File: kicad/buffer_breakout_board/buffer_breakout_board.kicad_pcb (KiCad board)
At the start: 4 copper layers, 44.7 x 44.6 mm, 46 parts, among them J1 Power, J2 Vcca_select, J3 In_Hi, J4 In_Lo, J5 Out_Hi, J6 Out_Lo, J7 Vccb_select, J8 JST_SH_BM04B-SRSS-TB, J9 Signals, U1 MCP4725A2T-E/CH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

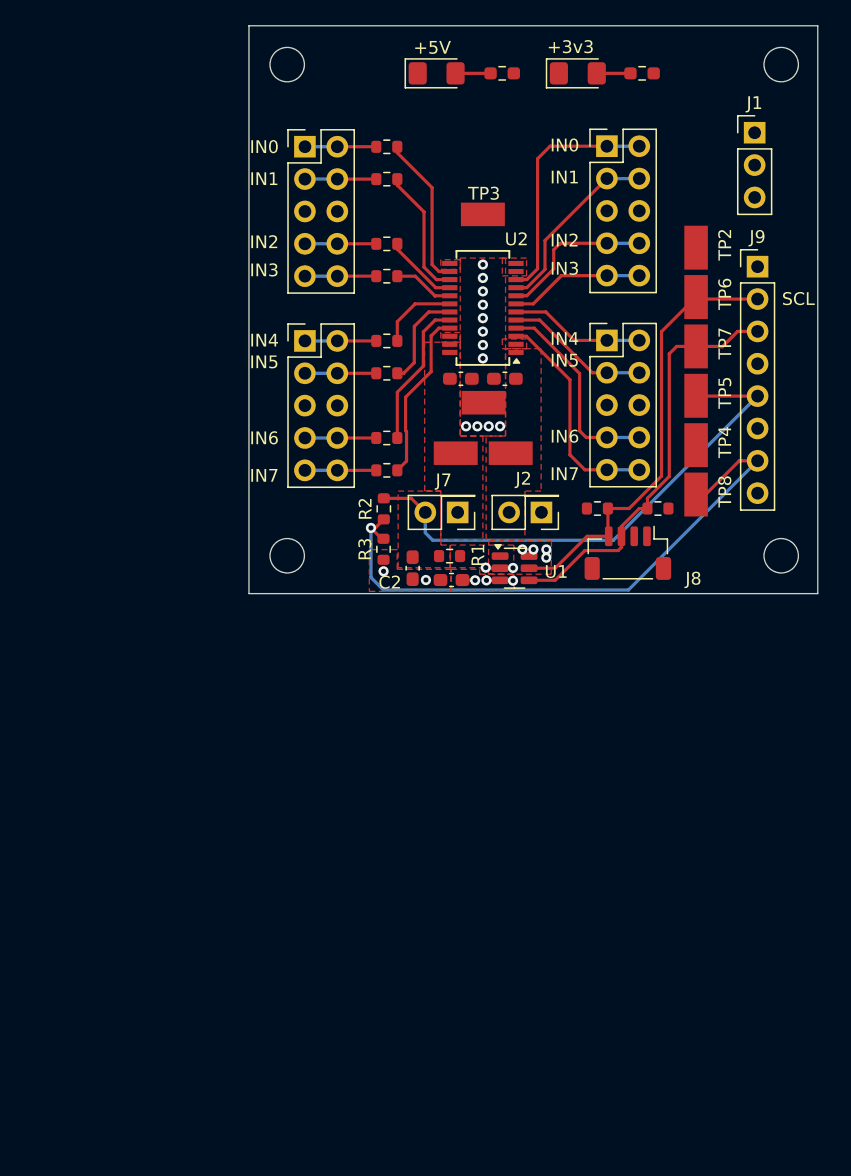
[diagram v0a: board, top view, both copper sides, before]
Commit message: renamed files, was working on wrong directory
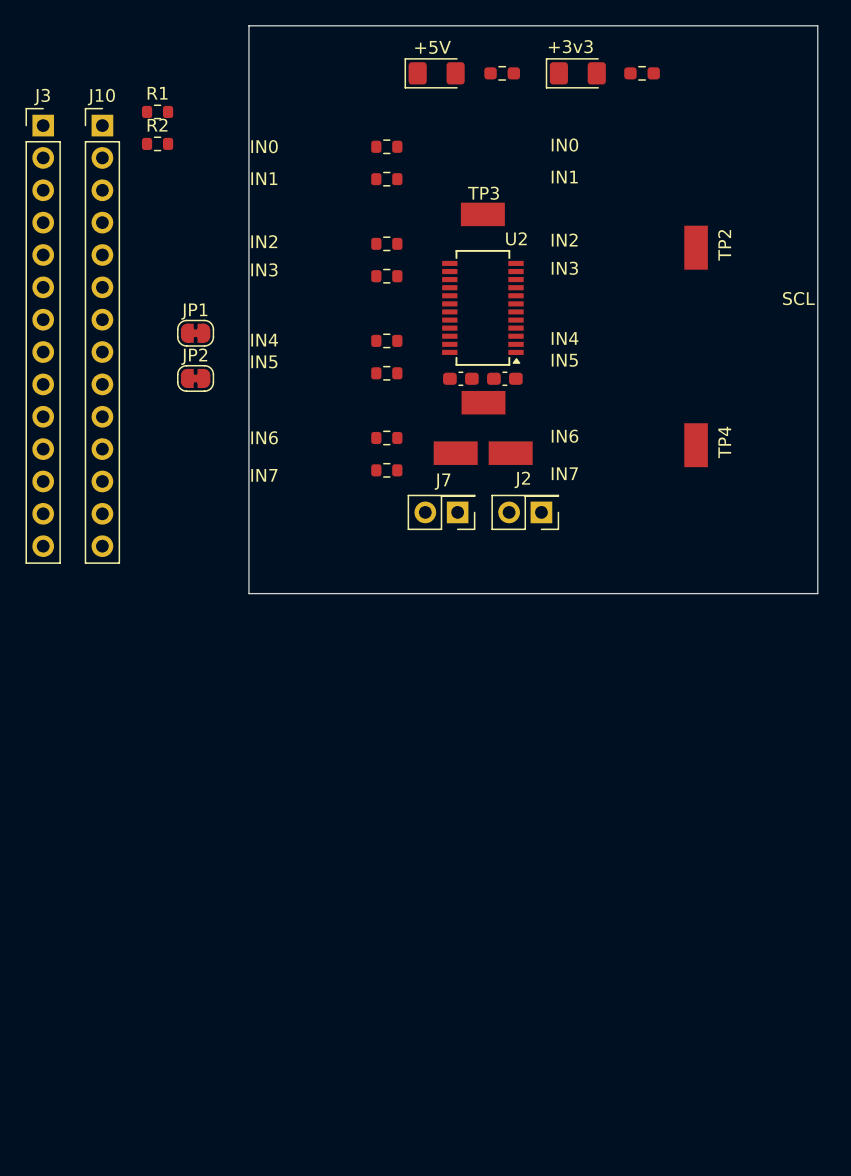
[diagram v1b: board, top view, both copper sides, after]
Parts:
- removed C1: 1u, Capacitor_SMD:C_0603_1608Metric_Pad1.08x0.95mm_HandSolder
- removed C2: 100n, Capacitor_SMD:C_0603_1608Metric_Pad1.08x0.95mm_HandSolder
- removed H1, H2, H3, H4: MountingHole, MountingHole:MountingHole_2.7mm
- removed J1: Power, Connector_PinHeader_2.54mm:PinHeader_1x03_P2.54mm_Vertical
- removed J4: In_Lo, Connector_PinHeader_2.54mm:PinHeader_2x05_P2.54mm_Vertical
- removed J5: Out_Hi, Connector_PinHeader_2.54mm:PinHeader_2x05_P2.54mm_Vertical
- removed J6: Out_Lo, Connector_PinHeader_2.54mm:PinHeader_2x05_P2.54mm_Vertical
- removed J8: JST_SH_BM04B-SRSS-TB, Connector_JST:JST_SH_BM04B-SRSS-TB_1x04-1MP_P1.00mm_Vertical
- removed J9: Signals, Connector_PinHeader_2.54mm:PinHeader_1x08_P2.54mm_Vertical
- removed R12, R13, R3: 10k, Resistor_SMD:R_0603_1608Metric
- removed TP5, TP6, TP7, TP8: TestPoint_Harwin, My Libraries:Harwin-S1751-46-Test-Point
- removed U1: MCP4725A2T-E/CH, Package_TO_SOT_SMD:SOT-23-6
- added J10: Data_In, Connector_PinHeader_2.54mm:PinHeader_1x14_P2.54mm_Vertical, F.Cu at (130.1, 83.3)
- added JP1: Jumper_2_Bridged, Jumper:SolderJumper-2_P1.3mm_Bridged_RoundedPad1.0x1.5mm, F.Cu at (137.5, 99.6)
- added JP2: Jumper_2_Bridged, Jumper:SolderJumper-2_P1.3mm_Bridged_RoundedPad1.0x1.5mm, F.Cu at (137.5, 103.2)
- D1: value 5V -> Vb
- D2: value 3v3 -> Va
- J3: value In_Hi -> Data_Out; footprint Connector_PinHeader_2.54mm:PinHeader_2x05_P2.54mm_Vertical -> Connector_PinHeader_2.54mm:PinHeader_1x14_P2.54mm_Vertical
- R1: value 0 -> 1k
- R2: value 10k -> 1k
- moved R1 41.7 mm to (134.5, 82.3), turned to 0 degrees
- moved R2 33.7 mm to (134.5, 84.8), turned to 0 degrees
- moved J3 26.6 mm to (125.5, 83.3)
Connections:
- J2 pad 1: +3V3 -> /Va_In
- J3 pad 1: /IN04 -> /Va_In
- J3 pad 10: /IN07 -> /BUF03
- J3 pad 2: /IN04 -> GND
- J3 pad 3: /IN05 -> /DIR
- J3 pad 4: /IN05 -> GND
- J3 pad 5: GND -> /BUF07
- J3 pad 6: GND -> /BUF06
- J3 pad 7: /IN06 -> /BUF05
- J3 pad 8: /IN06 -> /BUF04
- J3 pad 9: /IN07 -> GND
- J7 pad 2: /Vdac_out -> /Vb_In
- R1 pad 1: Net-(U1-VOUT) -> /DIR
- R1 pad 2: /Vdac_out -> GND
- R14 pad 1: +5V -> Net-(JP1-A)
- R15 pad 1: +3V3 -> Net-(JP2-A)
- R2 pad 1: /Vdac_half -> /OE
- R2 pad 2: /Vdac_out -> GND
- U2 pad 2: GND -> /DIR
- U2 pad 22: GND -> /OE
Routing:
- net /Vdac_half: track 47.4 -> 0.00 mm, vias 1 -> 0
- net /Vdac_out: track 41.2 -> 0.00 mm
- net /I2C1_SCL: track 34.8 -> 0.00 mm
- net /I2C1_SDA: track 33.1 -> 0.00 mm
- net /BUF00: track 19.1 -> 0.00 mm
- net /BUF07: track 17.5 -> 0.00 mm
- net /BUF06: track 15.9 -> 0.00 mm
- net /BUF01: track 14.6 -> 0.00 mm
- net /B7: track 13.4 -> 0.00 mm
- net /BUF02: track 12.3 -> 0.00 mm
- net /B0: track 12.0 -> 0.00 mm
- net /B6: track 11.6 -> 0.00 mm
- net /BUF05: track 11.4 -> 0.00 mm
- net /BUF04: track 10.6 -> 0.00 mm
- net /BUF03: track 10.6 -> 0.00 mm
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- removed copper zone on F.Cu, net +5V
- removed copper zone on F.Cu, net /Vdac_out
- removed copper zone on F.Cu, net GND
- removed copper zone on In1.Cu, net GND
- removed copper zone on F.Cu, net Net-(U1-VOUT)
- removed copper zone on F.Cu, net Vcca
- removed copper zone on F.Cu, net Vccb
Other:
- copper layers 4 -> 2

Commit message: floor planning attempt 1
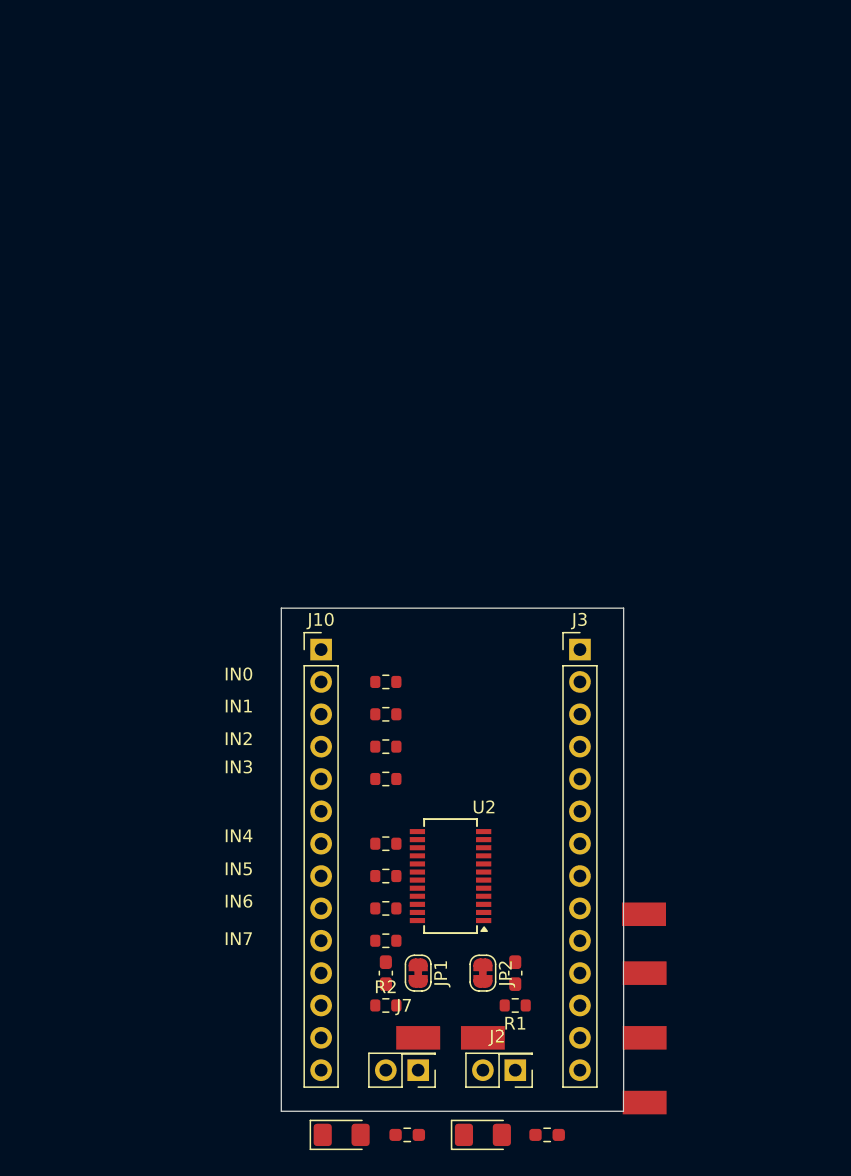
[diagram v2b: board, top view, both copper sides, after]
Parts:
- moved D1 83.7 mm to (148.9, 162.6)
- moved D2 83.7 mm to (160.0, 162.6)
- moved R14 83.7 mm to (154.1, 162.6)
- moved R15 83.7 mm to (165.1, 162.6)
- moved R1 75.6 mm to (162.6, 152.4), turned to 180 degrees
- moved R2 70.0 mm to (152.4, 152.4)
- moved TP2 67.2 mm to (172.7, 160.0), turned to 180 degrees
- moved J3 58.9 mm to (167.6, 124.5)
- moved TP3 56.4 mm to (172.7, 145.2)
- moved JP1 53.2 mm to (154.9, 149.9), turned to -90 degrees
- moved JP2 51.8 mm to (160.0, 149.9), turned to -90 degrees
- moved TP1 51.4 mm to (172.7, 154.9)
- moved C3 47.0 mm to (152.4, 149.9), turned to 90 degrees
- moved C4 46.7 mm to (162.6, 149.9), turned to 90 degrees
- moved TP10 46.0 mm to (154.9, 154.9)
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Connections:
- J10 pad 1: /Vb_In -> GND
- J10 pad 10: /IN03 -> /IN07
- J10 pad 11: /IN02 -> GND
- J10 pad 12: /IN01 -> /OE
- J10 pad 13: /IN00 -> GND
- J10 pad 14: GND -> /Vb_In
- J10 pad 2: GND -> /IN00
- J10 pad 3: /OE -> /IN01
- J10 pad 4: GND -> /IN02
- J10 pad 5: /IN07 -> /IN03
- J10 pad 6: /IN06 -> GND
- J10 pad 7: /IN05 -> /IN04
- J10 pad 8: /IN04 -> /IN05
- J10 pad 9: GND -> /IN06
- J3 pad 1: /Va_In -> GND
- J3 pad 10: /BUF03 -> /BUF07
- J3 pad 11: /BUF02 -> GND
- J3 pad 12: /BUF01 -> /DIR
- J3 pad 13: /BUF00 -> GND
- J3 pad 14: GND -> /Va_In
- J3 pad 2: GND -> /BUF00
- J3 pad 3: /DIR -> /BUF01
- J3 pad 4: GND -> /BUF02
- J3 pad 5: /BUF07 -> /BUF03
- J3 pad 6: /BUF06 -> GND
- J3 pad 7: /BUF05 -> /BUF04
- J3 pad 8: /BUF04 -> /BUF05
- J3 pad 9: GND -> /BUF06
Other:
- board size 44.7 x 44.6 mm -> 26.9 x 39.5 mm
- board text removed: "+3v3"
- board text removed: "+5V"
- board text removed: "SCL"

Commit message: drc passed rev1
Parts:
- added kibuzzard-67318B48: G***, kibuzzard-67318B48, B.Cu at (152.8, 90.6)
- moved TP4 65.6 mm to (159.0, 85.7)
- moved TP3 65.1 mm to (146.3, 85.7)
- moved TP1 63.6 mm to (152.9, 94.5)
- moved R15 45.2 mm to (158.0, 117.9), turned to 0 degrees
- moved R14 45.1 mm to (147.4, 117.9)
- moved TP10 44.6 mm to (150.1, 110.6)
- moved TP9 44.6 mm to (155.2, 110.6)
- moved TP2 44.3 mm to (152.7, 120.5)
- moved J2 43.4 mm to (157.5, 114.4)
- moved J7 43.4 mm to (150.2, 114.4)
- moved D2 42.2 mm to (157.3, 120.5)
- moved R2 42.1 mm to (145.6, 110.8), turned to 90 degrees
- moved D1 42.1 mm to (148.1, 120.5), turned to 180 degrees
- moved C4 41.9 mm to (155.2, 108.6), turned to 0 degrees
- moved R1 41.7 mm to (159.8, 110.8), turned to 90 degrees
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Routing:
- net /BUF00: track 0.00 -> 18.5 mm
- net /BUF01: track 0.00 -> 16.2 mm
- net /BUF02: track 0.00 -> 14.6 mm
- net /OE: track 0.00 -> 14.3 mm
- net /DIR: track 0.00 -> 13.9 mm
- net /B0: track 0.00 -> 13.0 mm
- net /BUF03: track 0.00 -> 12.6 mm
- net /B1: track 0.00 -> 11.8 mm
- net /B2: track 0.00 -> 9.17 mm
- net /BUF07: track 0.00 -> 9.12 mm
- net GND: track 0.00 -> 9.07 mm, vias 0 -> 21
- net /BUF06: track 0.00 -> 8.33 mm
- net /BUF04: track 0.00 -> 8.06 mm
- net /BUF05: track 0.00 -> 7.54 mm
- net /B3: track 0.00 -> 7.38 mm
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- added copper zone on F.Cu, net /Va_In
- added copper zone on F.Cu, net /Vb_In
- added copper zone on B.Cu, net GND
- added copper zone on F.Cu, net GND
- added copper zone on F.Cu, net Net-(JP1-A)
- added copper zone on F.Cu, net Net-(JP2-A)
- added copper zone on F.Cu, net Vcca
- added copper zone on F.Cu, net Vccb
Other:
- board size 26.9 x 39.5 mm -> 24.1 x 38.1 mm
- board text removed: "IN0"
- board text removed: "IN1"
- board text removed: "IN2"
- board text removed: "IN3"
- board text removed: "IN4"
- board text removed: "IN5"
- board text removed: "IN6"
- board text removed: "IN7"
